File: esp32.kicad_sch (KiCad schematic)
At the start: 34 parts, among them J3 TC2030-IDC, J7 Conn_01x04, J8 USB_C_Receptacle_USB2.0, Q5 BSS123, SW1 EVQ-9P701P, U3 176x320_st7789, U7 SN74AVC4T774, U9 ESP32-S3-WROOM-1, Y1 32.768kHz

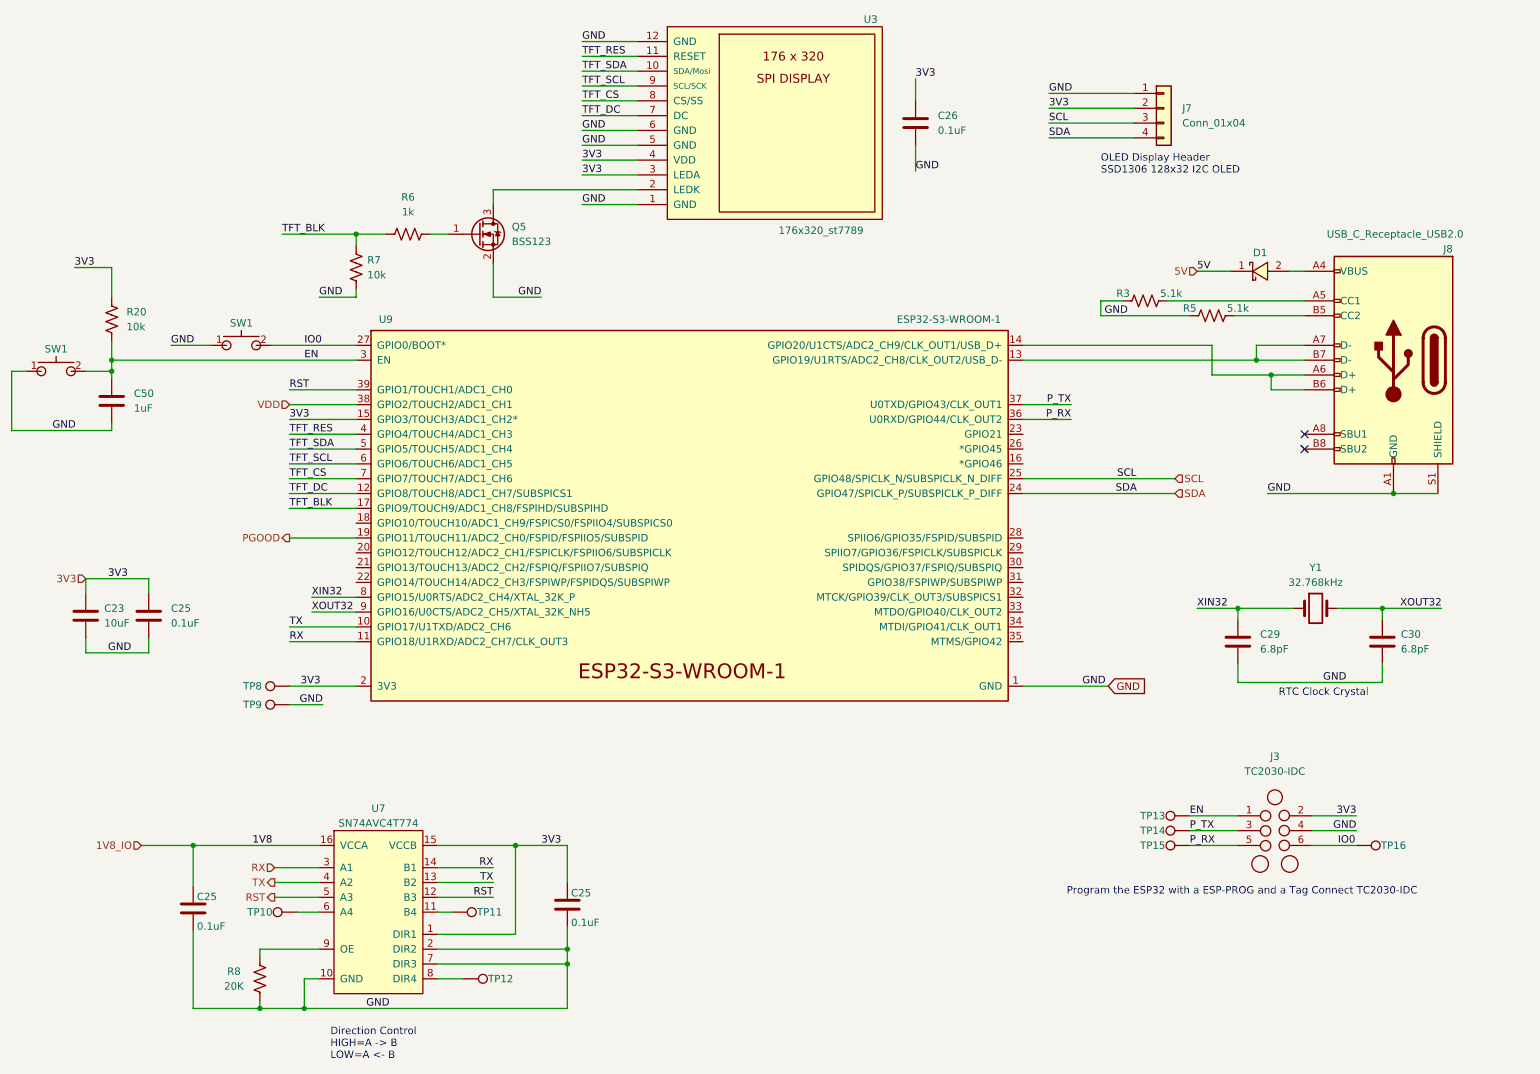
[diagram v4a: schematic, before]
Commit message: Routing of front end ESP32, power supply, fan controller, level translator, and programming connector
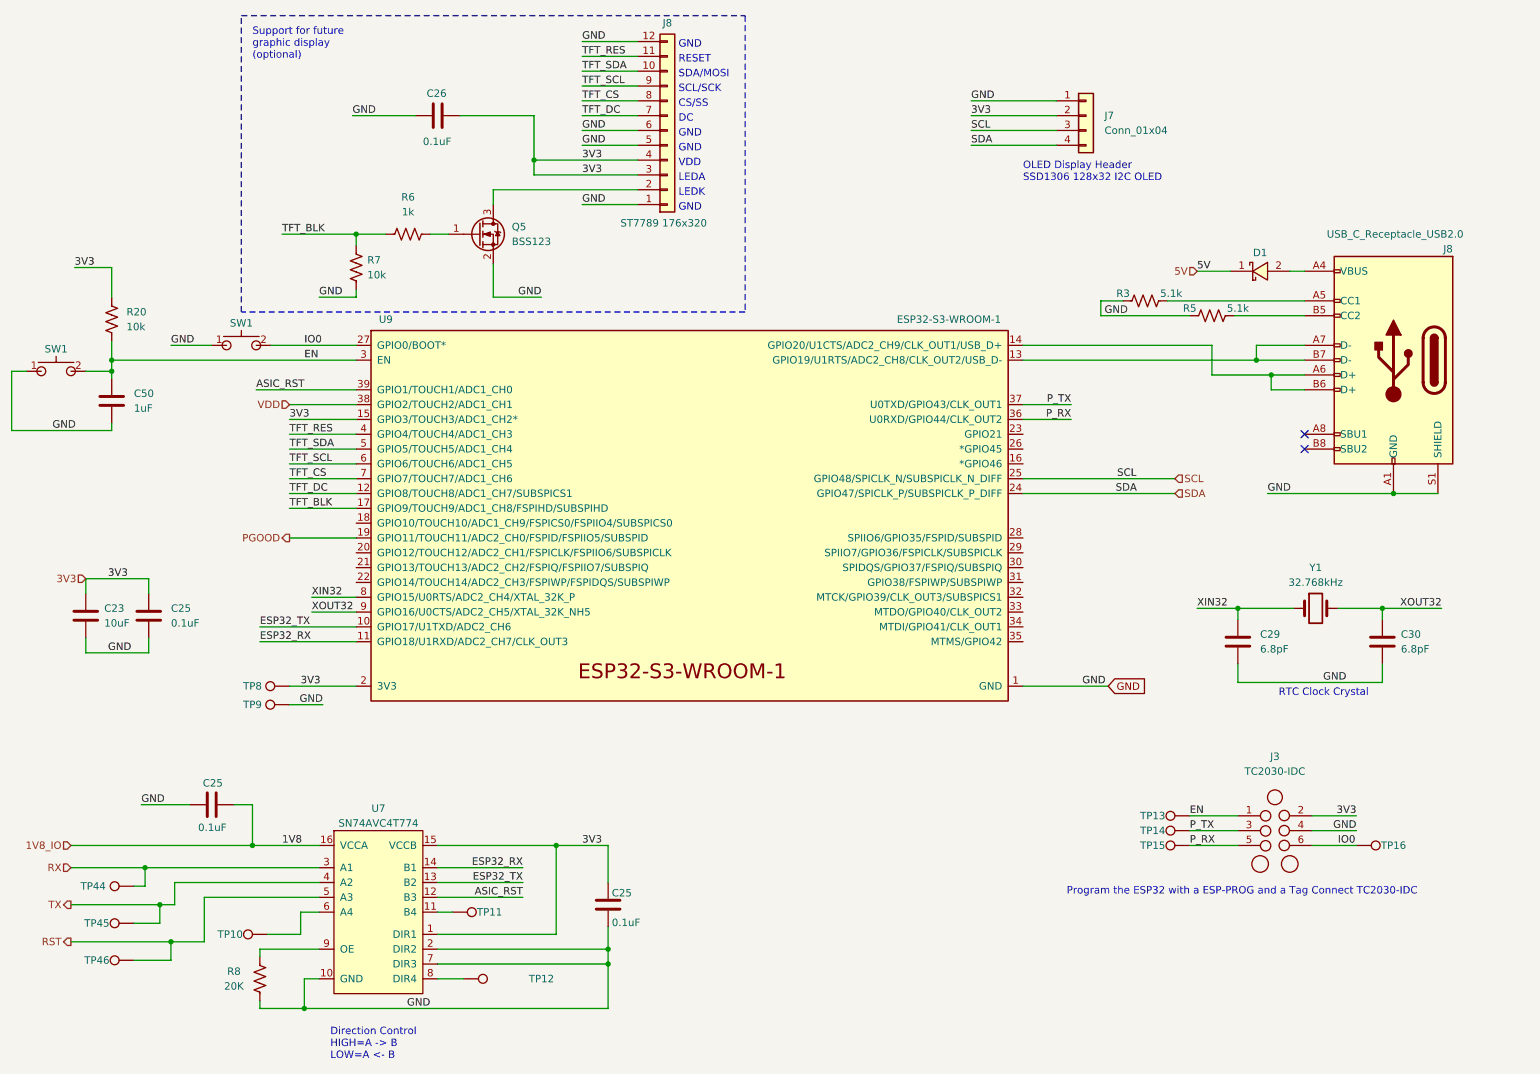
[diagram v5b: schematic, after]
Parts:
- removed U3: 176x320_st7789, Connector_PinHeader_2.54mm:PinHeader_2x06_P2.54mm_Vertical, symbol bitaxe:176x320_st7789
- added J8: ST7789 176x320, Connector_JST:JST_GH_BM12B-GHS-TBT_1x12-1MP_P1.25mm_Vertical, symbol Connector_Generic:Conn_01x12
- added TP44, TP45, TP46: TestPoint, TestPoint:TestPoint_Pad_D1.0mm, symbol Connector:TestPoint
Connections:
- net 1V8_IO: now also C25.2; no longer C25.1
- net 3V3: now also J8.3 (Pin_3), J8.4 (Pin_4)
- net GND: now also C25.1, J8.1 (Pin_1), J8.12 (Pin_12), J8.5 (Pin_5), J8.6 (Pin_6); no longer C25.2
- net RST: now also TP46.1; no longer U7.12 (B3), U9.39 (GPIO1/TOUCH1/ADC1_CH0)
- net RX: now also TP44.1; no longer U7.14 (B1), U9.11 (GPIO18/U1RXD/ADC2_CH7/CLK_OUT3)
- net TFT_CS: now also J8.8 (Pin_8)
- net TFT_DC: now also J8.7 (Pin_7)
- net TFT_RES: now also J8.11 (Pin_11)
- net TFT_SCL: now also J8.9 (Pin_9)
- net TFT_SDA: now also J8.10 (Pin_10)
- net TX: now also TP45.1; no longer U7.13 (B2), U9.10 (GPIO17/U1TXD/ADC2_CH6)
- net at Q5.3 (D): now also J8.2 (Pin_2)
- new net ASIC_RST: U7.12 (B3), U9.39 (GPIO1/TOUCH1/ADC1_CH0)
- new net ESP32_RX: U7.14 (B1), U9.11 (GPIO18/U1RXD/ADC2_CH7/CLK_OUT3)
- new net ESP32_TX: U7.13 (B2), U9.10 (GPIO17/U1TXD/ADC2_CH6)
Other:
- note added: "CS/SS"
- note added: "DC"
- note added: "GND"
- note added: "LEDA"
- note added: "LEDK"
- note added: "RESET"
- note added: "SCL/SCK"
- note added: "SDA/MOSI"
- note added: "Support for future graphic display (optional)"
- note added: "VDD"
- moved on the sheet: C25, C26, J7, TP10

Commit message: added some models and regenerated the board render
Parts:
- SW1: DK (none) -> P19095CT-ND; PARTNO (none) -> EVQ-9P701P
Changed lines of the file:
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@@
+      (effects (font (size 1.27 1.27)) hide)
+    )
+    (property "PARTNO" "EVQ-9P701P" (at 21.59 75.565 0)
+      (effects (font (size 1.27 1.27)) hide)
+    )
+    (property "DK" "P19095CT-ND" (at 21.59 75.565 0)
       (effects (font (size 1.27 1.27)) hide)
     )
@@
       (effects (font (size 1.27 1.27)) hide)
     )
+    (property "DK" "P19095CT-ND" (at 53.34 71.12 0)
+      (effects (font (size 1.27 1.27)) hide)
+    )
+    (property "PARTNO" "EVQ-9P701P" (at 53.34 71.12 0)
+      (effects (font (size 1.27 1.27)) hide)
+    )

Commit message: added some DK part numbers
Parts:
- J8: DK (none) -> 455-BM12B-GHS-TBTCT-ND; PARTNO (none) -> BM12B-GHS-TBT
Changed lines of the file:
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@@
+      (effects (font (size 1.27 1.27)) hide)
+    )
+    (property "PARTNO" "BM12B-GHS-TBT" (at 126.365 34.29 0)
+      (effects (font (size 1.27 1.27)) hide)
+    )
+    (property "DK" "455-BM12B-GHS-TBTCT-ND" (at 126.365 34.29 0)
       (effects (font (size 1.27 1.27)) hide)
     )
